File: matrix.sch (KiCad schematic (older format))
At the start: 134 parts, among them SW1 SW_Push, SW10 SW_Push, SW11 SW_Push, SW12 SW_Push, SW13 SW_Push, SW14 SW_Push, SW15 SW_Push, SW16 SW_Push, SW17 SW_Push, SW18 SW_Push, SW19 SW_Push, SW2 SW_Push, SW20 SW_Push, SW21 SW_Push, SW22 SW_Push, SW23 SW_Push, SW24 SW_Push, SW25 SW_Push, SW26 SW_Push, SW27 SW_Push, SW28 SW_Push, SW29 SW_Push, SW3 SW_Push, SW30 SW_Push, SW31 SW_Push, SW32 SW_Push, SW33 SW_Push, SW34 SW_Push, SW35 SW_Push, SW36 SW_Push, SW37 SW_Push, SW38 SW_Push, SW39 SW_Push, SW4 SW_Push, SW40 SW_Push, SW41 SW_Push, SW42 SW_Push, SW43 SW_Push, SW44 SW_Push, SW45 SW_Push, SW46 SW_Push, SW47 SW_Push, SW48 SW_Push, SW49 SW_Push, SW5 SW_Push, SW50 SW_Push, SW51 SW_Push, SW52 SW_Push, SW53 SW_Push, SW54 SW_Push, SW55 SW_Push, SW56 SW_Push, SW57 SW_Push, SW58 SW_Push, SW59 SW_Push, SW6 SW_Push, SW60 SW_Push, SW61 SW_Push, SW62 SW_Push, SW63 SW_Push, SW64 SW_Push, SW65 SW_Push, SW66 SW_Push, SW67 SW_Push, SW7 SW_Push, SW8 SW_Push, SW9 SW_Push

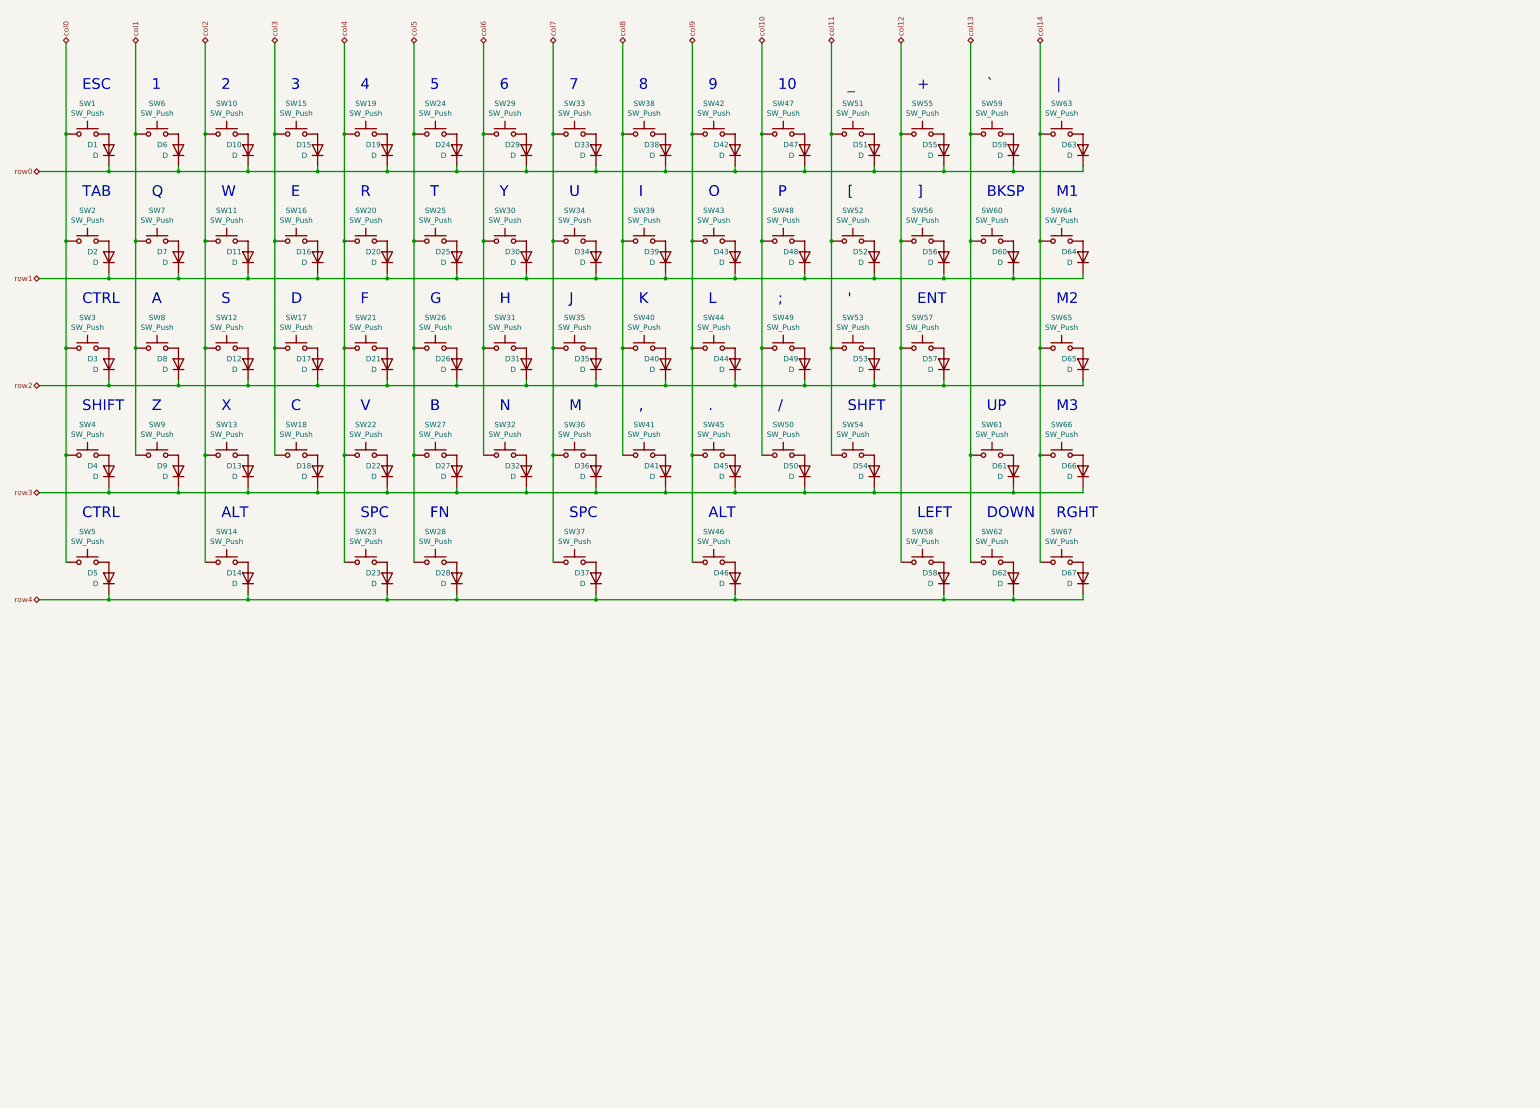
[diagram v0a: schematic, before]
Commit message: added footprints
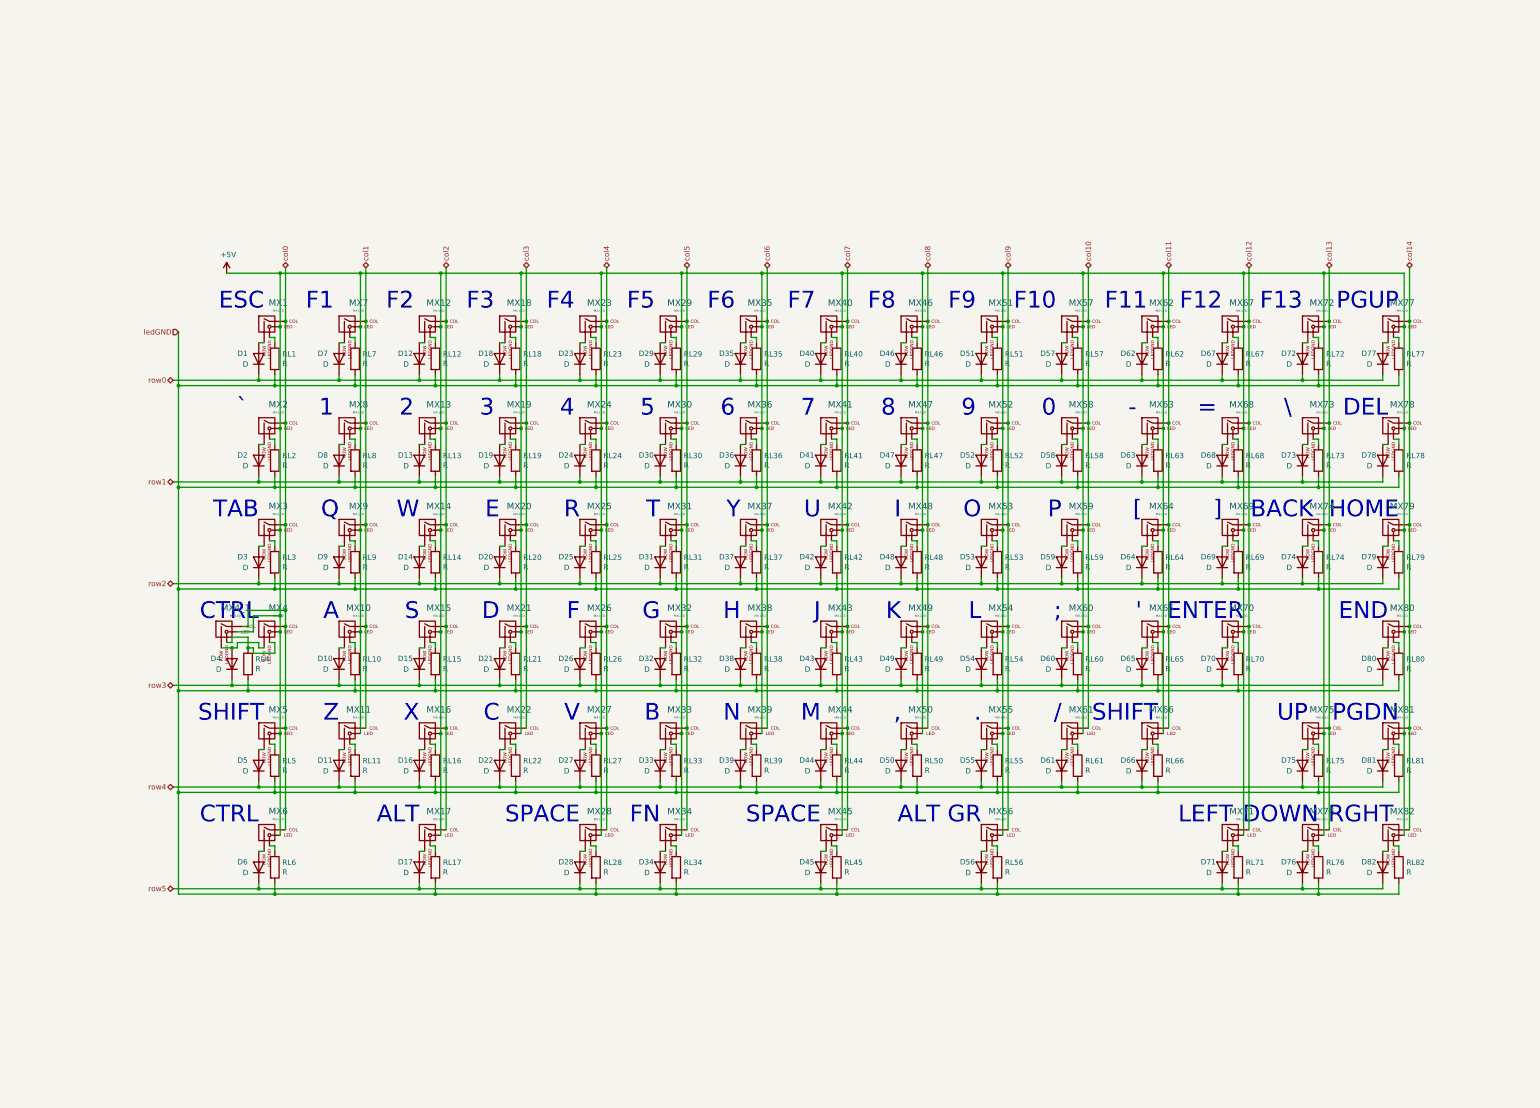
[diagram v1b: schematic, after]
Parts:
- removed SW1, SW10, SW11, SW12, SW13, SW15, SW16, SW17, SW18, SW19, SW20, SW21, SW22, SW24, SW25, SW26, SW27, SW28, SW29, SW30, SW31, SW32, SW33, SW34, SW35, SW36, SW38, SW39, SW40, SW41, SW42, SW43, SW44, SW45, SW47, SW48, SW49, SW50, SW51, SW52, SW53, SW55, SW56, SW58, SW59, SW6, SW61, SW62, SW63, SW64, SW65, SW66, SW67, SW7, SW8, SW9: SW_Push, Fate_Parts:SW_Cherry_MX_1.00u_PCB, symbol Switch:SW_Push
- removed SW14, SW2, SW46, SW5, SW60: SW_Push, Fate_Parts:SW_Cherry_MX_1.50u_PCB, symbol Switch:SW_Push
- removed SW23: SW_Push, Fate_Parts:SW_Cherry_MX_2.00u_PCB_ReversedStabilizers, symbol Switch:SW_Push
- removed SW3, SW54: SW_Push, Fate_Parts:SW_Cherry_MX_1.75u_PCB, symbol Switch:SW_Push
- removed SW37: SW_Push, Fate_Parts:SW_Cherry_MX_2.75u_PCB_ReversedStabilizers, symbol Switch:SW_Push
- removed SW4: SW_Push, Fate_Parts:SW_Cherry_MX_2.25u_PCB, symbol Switch:SW_Push
- removed SW57: SW_Push, Fate_Parts:SW_Cherry_MX_2.25u_PCB_ReversedStabilizers, symbol Switch:SW_Push
- added D68, D69, D70, D71, D72, D73, D74, D75, D76, D77, D78, D79, D80, D81, D82: D, Diode_SMD:D_SOD-123, symbol Device:D
- added MX1, MX10, MX11, MX12, MX13, MX14, MX15, MX16, MX18, MX19, MX2, MX20, MX21, MX22, MX23, MX24, MX25, MX26, MX27, MX29, MX30, MX31, MX32, MX33, MX34, MX35, MX36, MX37, MX38, MX39, MX40, MX41, MX42, MX43, MX44, MX46, MX47, MX48, MX49, MX50, MX51, MX52, MX53, MX54, MX55, MX57, MX58, MX59, MX60, MX61, MX62, MX63, MX64, MX65, MX67, MX68, MX69, MX7, MX71, MX72, MX73, MX75, MX76, MX77, MX78, MX79, MX8, MX80, MX81, MX82, MX9: MX-LED, ai03-MX_only:MXOnly-1U, symbol ai03-schematic_library:MX-LED
- added MX17, MX3, MX56, MX6, MX74: MX-LED, ai03-MX_only:MXOnly-1.5U, symbol ai03-schematic_library:MX-LED
- added MX28: MX-LED, ai03-MX_only:MXOnly-2U-FLIPPED-ReversedStabilizers, symbol ai03-schematic_library:MX-LED
- added MX4, MX66: MX-LED, ai03-MX_only:MXOnly-1.75U, symbol ai03-schematic_library:MX-LED
- added MX45: MX-LED, ai03-MX_only:MXOnly-2.75U-ReversedStabilizers, symbol ai03-schematic_library:MX-LED
- added MX4_1: MX-LED, ai03-MX_only:MXOnly-1.75U-FLIPPED, symbol ai03-schematic_library:MX-LED
- added MX5: MX-LED, ai03-MX_only:MXOnly-2.25U, symbol ai03-schematic_library:MX-LED
- added MX70: MX-LED, ai03-MX_only:MXOnly-2.25U-FLIPPED-ReversedStabilizers, symbol ai03-schematic_library:MX-LED
- added RL1, RL10, RL11, RL12, RL13, RL14, RL15, RL16, RL17, RL18, RL19, RL2, RL20, RL21, RL22, RL23, RL24, RL25, RL26, RL27, RL28, RL29, RL3, RL30, RL31, RL32, RL33, RL34, RL35, RL36, RL37, RL38, RL39, RL4, RL40, RL41, RL42, RL43, RL44, RL45, RL46, RL47, RL48, RL49, RL5, RL50, RL51, RL52, RL53, RL54, RL55, RL56, RL57, RL58, RL59, RL6, RL60, RL61, RL62, RL63, RL64, RL65, RL66, RL67, RL68, RL69, RL7, RL70, RL71, RL72, RL73, RL74, RL75, RL76, RL77, RL78, RL79, RL8, RL80, RL81, RL82, RL9: R, Resistor_SMD:R_0805_2012Metric_Pad1.15x1.40mm_HandSolder, symbol Device:R
- D1, D10, D11, D12, D13, D14, D15, D16, D17, D18, D19, D2, D20, D21, D22, D23, D24, D25, D26, D27, D28, D29, D3, D30, D31, D32, D33, D34, D35, D36, D37, D38, D39, D4, D40, D41, D42, D43, D44, D45, D46, D47, D48, D49, D5, D50, D51, D52, D53, D54, D55, D56, D57, D58, D59, D6, D60, D61, D62, D63, D64, D65, D66, D67, D7, D8, D9: footprint Diodes_SMD:D_SOD-123 -> Diode_SMD:D_SOD-123
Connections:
- net col0: now also MX1.1 (COL), MX2.1 (COL), MX3.1 (COL), MX4.1 (COL), MX4_1.1 (COL), MX5.1 (COL), MX6.1 (COL)
- net col1: now also MX10.1 (COL), MX11.1 (COL), MX7.1 (COL), MX8.1 (COL), MX9.1 (COL)
- net col10: now also MX57.1 (COL), MX58.1 (COL), MX59.1 (COL), MX60.1 (COL), MX61.1 (COL)
- net col11: now also MX62.1 (COL), MX63.1 (COL), MX64.1 (COL), MX65.1 (COL), MX66.1 (COL)
- net col12: now also MX67.1 (COL), MX68.1 (COL), MX69.1 (COL), MX70.1 (COL), MX71.1 (COL)
- net col13: now also MX72.1 (COL), MX73.1 (COL), MX74.1 (COL), MX75.1 (COL), MX76.1 (COL)
- net col14: now also MX77.1 (COL), MX78.1 (COL), MX79.1 (COL), MX80.1 (COL), MX81.1 (COL), MX82.1 (COL)
- net col2: now also MX12.1 (COL), MX13.1 (COL), MX14.1 (COL), MX15.1 (COL), MX16.1 (COL), MX17.1 (COL)
- net col3: now also MX18.1 (COL), MX19.1 (COL), MX20.1 (COL), MX21.1 (COL), MX22.1 (COL)
- net col4: now also MX23.1 (COL), MX24.1 (COL), MX25.1 (COL), MX26.1 (COL), MX27.1 (COL), MX28.1 (COL)
- net col5: now also MX29.1 (COL), MX30.1 (COL), MX31.1 (COL), MX32.1 (COL), MX33.1 (COL), MX34.1 (COL)
- net col6: now also MX35.1 (COL), MX36.1 (COL), MX37.1 (COL), MX38.1 (COL), MX39.1 (COL)
- net col7: now also MX40.1 (COL), MX41.1 (COL), MX42.1 (COL), MX43.1 (COL), MX44.1 (COL), MX45.1 (COL)
- net col8: now also MX46.1 (COL), MX47.1 (COL), MX48.1 (COL), MX49.1 (COL), MX50.1 (COL)
- net col9: now also MX51.1 (COL), MX52.1 (COL), MX53.1 (COL), MX54.1 (COL), MX55.1 (COL), MX56.1 (COL)
- net row0: now also D12.1 (K), D18.1 (K), D23.1 (K), D35.1 (K), D40.1 (K), D46.1 (K), D57.1 (K), D62.1 (K), D67.1 (K), D7.1 (K), D72.1 (K), D77.1 (K); no longer D10.1 (K), D15.1 (K), D19.1 (K), D24.1 (K), D33.1 (K), D38.1 (K), D42.1 (K), D47.1 (K), D55.1 (K), D59.1 (K), D6.1 (K), D63.1 (K)
- net row1: now also D13.1 (K), D19.1 (K), D24.1 (K), D36.1 (K), D41.1 (K), D47.1 (K), D58.1 (K), D63.1 (K), D8.1 (K), D68.1 (K), D73.1 (K), D78.1 (K); no longer D11.1 (K), D16.1 (K), D20.1 (K), D25.1 (K), D34.1 (K), D39.1 (K), D43.1 (K), D48.1 (K), D56.1 (K), D60.1 (K), D64.1 (K), D7.1 (K)
- net row2: now also D14.1 (K), D20.1 (K), D25.1 (K), D37.1 (K), D42.1 (K), D48.1 (K), D59.1 (K), D64.1 (K), D9.1 (K), D69.1 (K), D74.1 (K), D79.1 (K); no longer D12.1 (K), D17.1 (K), D21.1 (K), D26.1 (K), D35.1 (K), D40.1 (K), D44.1 (K), D49.1 (K), D57.1 (K), D65.1 (K), D8.1 (K)
- net row3: now also D10.1 (K), D15.1 (K), D21.1 (K), D26.1 (K), D38.1 (K), D43.1 (K), D49.1 (K), D60.1 (K), D65.1 (K), D70.1 (K), D80.1 (K); no longer D13.1 (K), D18.1 (K), D22.1 (K), D27.1 (K), D36.1 (K), D41.1 (K), D45.1 (K), D50.1 (K), D61.1 (K), D66.1 (K), D9.1 (K)
- net row4: now also D11.1 (K), D16.1 (K), D22.1 (K), D27.1 (K), D33.1 (K), D39.1 (K), D44.1 (K), D50.1 (K), D55.1 (K), D61.1 (K), D66.1 (K), D75.1 (K), D81.1 (K); no longer D14.1 (K), D23.1 (K), D28.1 (K), D37.1 (K), D46.1 (K), D58.1 (K), D62.1 (K), D67.1 (K)
- net at D1.2 (A): now also MX1.2 (ROW)
- net at D6.2 (A): now also MX6.2 (ROW)
- net at D2.2 (A): now also MX2.2 (ROW)
- net at D7.2 (A): now also MX7.2 (ROW)
- net at D3.2 (A): now also MX3.2 (ROW)
- net at D4.2 (A): now also MX4.2 (ROW), MX4_1.2 (ROW)
- net at D5.2 (A): now also MX5.2 (ROW)
- net at D8.2 (A): now also MX8.2 (ROW)
- net at D9.2 (A): now also MX9.2 (ROW)
- net at D10.2 (A): now also MX10.2 (ROW)
- net at D11.2 (A): now also MX11.2 (ROW)
- net at D12.2 (A): now also MX12.2 (ROW)
- net at D13.2 (A): now also MX13.2 (ROW)
- net at D14.2 (A): now also MX14.2 (ROW)
- net at D15.2 (A): now also MX15.2 (ROW)
- net at D16.2 (A): now also MX16.2 (ROW)
- net at D17.2 (A): now also MX17.2 (ROW)
- net at D18.2 (A): now also MX18.2 (ROW)
- net at D19.2 (A): now also MX19.2 (ROW)
- net at D20.2 (A): now also MX20.2 (ROW)
- net at D21.2 (A): now also MX21.2 (ROW)
- net at D22.2 (A): now also MX22.2 (ROW)
- net at D23.2 (A): now also MX23.2 (ROW)
- net at D24.2 (A): now also MX24.2 (ROW)
- net at D25.2 (A): now also MX25.2 (ROW)
- net at D26.2 (A): now also MX26.2 (ROW)
- net at D27.2 (A): now also MX27.2 (ROW)
- net at D28.2 (A): now also MX28.2 (ROW)
- net at D29.2 (A): now also MX29.2 (ROW)
- net at D30.2 (A): now also MX30.2 (ROW)
- net at D31.2 (A): now also MX31.2 (ROW)
- net at D32.2 (A): now also MX32.2 (ROW)
- net at D33.2 (A): now also MX33.2 (ROW)
- net at D34.2 (A): now also MX34.2 (ROW)
- net at D35.2 (A): now also MX35.2 (ROW)
- net at D36.2 (A): now also MX36.2 (ROW)
- net at D37.2 (A): now also MX37.2 (ROW)
- net at D38.2 (A): now also MX38.2 (ROW)
- net at D39.2 (A): now also MX39.2 (ROW)
- net at D40.2 (A): now also MX40.2 (ROW)
- net at D41.2 (A): now also MX41.2 (ROW)
- net at D42.2 (A): now also MX42.2 (ROW)
- net at D43.2 (A): now also MX43.2 (ROW)
- net at D44.2 (A): now also MX44.2 (ROW)
- net at D45.2 (A): now also MX45.2 (ROW)
- net at D46.2 (A): now also MX46.2 (ROW)
- net at D47.2 (A): now also MX47.2 (ROW)
- net at D48.2 (A): now also MX48.2 (ROW)
- net at D49.2 (A): now also MX49.2 (ROW)
- net at D50.2 (A): now also MX50.2 (ROW)
- net at D51.2 (A): now also MX51.2 (ROW)
- net at D52.2 (A): now also MX52.2 (ROW)
- net at D53.2 (A): now also MX53.2 (ROW)
- net at D54.2 (A): now also MX54.2 (ROW)
- net at D55.2 (A): now also MX55.2 (ROW)
- net at D56.2 (A): now also MX56.2 (ROW)
- net at D57.2 (A): now also MX57.2 (ROW)
- net at D58.2 (A): now also MX58.2 (ROW)
- net at D59.2 (A): now also MX59.2 (ROW)
- net at D60.2 (A): now also MX60.2 (ROW)
- net at D61.2 (A): now also MX61.2 (ROW)
- net at D62.2 (A): now also MX62.2 (ROW)
- net at D63.2 (A): now also MX63.2 (ROW)
- net at D64.2 (A): now also MX64.2 (ROW)
- net at D65.2 (A): now also MX65.2 (ROW)
- net at D66.2 (A): now also MX66.2 (ROW)
- net at D67.2 (A): now also MX67.2 (ROW)
- new net: MX4.4 (LEDGND), MX4_1.4 (LEDGND), RL4.1
- new net: MX1.4 (LEDGND), RL1.1
- new net: MX7.4 (LEDGND), RL7.1
- new net: MX12.4 (LEDGND), RL12.1
- new net: MX18.4 (LEDGND), RL18.1
- new net: MX40.4 (LEDGND), RL40.1
- new net: MX35.4 (LEDGND), RL35.1
- new net: MX23.4 (LEDGND), RL23.1
- new net: MX29.4 (LEDGND), RL29.1
- new net: MX62.4 (LEDGND), RL62.1
- new net: MX57.4 (LEDGND), RL57.1
- new net: MX46.4 (LEDGND), RL46.1
- new net: MX51.4 (LEDGND), RL51.1
- new net: D77.2 (A), MX77.2 (ROW)
- new net: MX77.4 (LEDGND), RL77.1
- new net: MX67.4 (LEDGND), RL67.1
- new net: D72.2 (A), MX72.2 (ROW)
- new net: MX72.4 (LEDGND), RL72.1
- new net: MX5.4 (LEDGND), RL5.1
- new net: D78.2 (A), MX78.2 (ROW)
- new net: MX68.4 (LEDGND), RL68.1
- new net: MX73.4 (LEDGND), RL73.1
- new net: MX78.4 (LEDGND), RL78.1
- new net: D68.2 (A), MX68.2 (ROW)
- new net: D73.2 (A), MX73.2 (ROW)
- new net: MX58.4 (LEDGND), RL58.1
- new net: MX52.4 (LEDGND), RL52.1
- new net: MX47.4 (LEDGND), RL47.1
- new net: MX19.4 (LEDGND), RL19.1
- new net: MX30.4 (LEDGND), RL30.1
- new net: MX24.4 (LEDGND), RL24.1
- new net: MX63.4 (LEDGND), RL63.1
- new net: MX36.4 (LEDGND), RL36.1
- new net: MX13.4 (LEDGND), RL13.1
- new net: MX41.4 (LEDGND), RL41.1
- new net: MX2.4 (LEDGND), RL2.1
- new net: MX8.4 (LEDGND), RL8.1
- new net: D79.2 (A), MX79.2 (ROW)
- new net: MX69.4 (LEDGND), RL69.1
- new net: MX74.4 (LEDGND), RL74.1
- new net: MX79.4 (LEDGND), RL79.1
- new net: D69.2 (A), MX69.2 (ROW)
- new net: D74.2 (A), MX74.2 (ROW)
- new net: MX59.4 (LEDGND), RL59.1
- new net: MX53.4 (LEDGND), RL53.1
- new net: MX48.4 (LEDGND), RL48.1
- new net: MX20.4 (LEDGND), RL20.1
- new net: MX31.4 (LEDGND), RL31.1
- new net: MX25.4 (LEDGND), RL25.1
- new net: MX64.4 (LEDGND), RL64.1
- new net: MX37.4 (LEDGND), RL37.1
- new net: MX14.4 (LEDGND), RL14.1
- new net: MX42.4 (LEDGND), RL42.1
- new net: MX3.4 (LEDGND), RL3.1
- new net: MX9.4 (LEDGND), RL9.1
- new net: D80.2 (A), MX80.2 (ROW)
- new net: MX70.4 (LEDGND), RL70.1
- new net: MX80.4 (LEDGND), RL80.1
- new net: D70.2 (A), MX70.2 (ROW)
- new net: MX60.4 (LEDGND), RL60.1
- new net: MX54.4 (LEDGND), RL54.1
- new net: MX49.4 (LEDGND), RL49.1
- new net: MX21.4 (LEDGND), RL21.1
- new net: MX32.4 (LEDGND), RL32.1
- new net: MX26.4 (LEDGND), RL26.1
- new net: MX65.4 (LEDGND), RL65.1
- new net: MX38.4 (LEDGND), RL38.1
- new net: MX15.4 (LEDGND), RL15.1
- new net: MX43.4 (LEDGND), RL43.1
- new net: MX10.4 (LEDGND), RL10.1
- new net: D81.2 (A), MX81.2 (ROW)
- new net: MX75.4 (LEDGND), RL75.1
- new net: MX81.4 (LEDGND), RL81.1
- new net: D75.2 (A), MX75.2 (ROW)
- new net: MX61.4 (LEDGND), RL61.1
- new net: MX55.4 (LEDGND), RL55.1
- new net: MX50.4 (LEDGND), RL50.1
- new net: MX22.4 (LEDGND), RL22.1
- new net: MX33.4 (LEDGND), RL33.1
- new net: MX27.4 (LEDGND), RL27.1
- new net: MX66.4 (LEDGND), RL66.1
- new net: MX39.4 (LEDGND), RL39.1
- new net: MX16.4 (LEDGND), RL16.1
- new net: MX44.4 (LEDGND), RL44.1
- new net: MX11.4 (LEDGND), RL11.1
- new net: D82.2 (A), MX82.2 (ROW)
- new net: MX71.4 (LEDGND), RL71.1
- new net: MX76.4 (LEDGND), RL76.1
- new net: MX82.4 (LEDGND), RL82.1
- new net: D71.2 (A), MX71.2 (ROW)
- new net: D76.2 (A), MX76.2 (ROW)
- new net: MX56.4 (LEDGND), RL56.1
- new net: MX34.4 (LEDGND), RL34.1
- new net: MX28.4 (LEDGND), RL28.1
- new net: MX17.4 (LEDGND), RL17.1
- new net: MX45.4 (LEDGND), RL45.1
- new net: MX6.4 (LEDGND), RL6.1
- new net +5V: MX1.3 (LED), MX10.3 (LED), MX11.3 (LED), MX12.3 (LED), MX13.3 (LED), MX14.3 (LED), MX15.3 (LED), MX16.3 (LED), MX17.3 (LED), MX18.3 (LED), MX19.3 (LED), MX2.3 (LED), MX20.3 (LED), MX21.3 (LED), MX22.3 (LED), MX23.3 (LED), MX24.3 (LED), MX25.3 (LED), MX26.3 (LED), MX27.3 (LED), MX28.3 (LED), MX29.3 (LED), MX3.3 (LED), MX30.3 (LED), MX31.3 (LED), MX32.3 (LED), MX33.3 (LED), MX34.3 (LED), MX35.3 (LED), MX36.3 (LED), MX37.3 (LED), MX38.3 (LED), MX39.3 (LED), MX4.3 (LED), MX40.3 (LED), MX41.3 (LED), MX42.3 (LED), MX43.3 (LED), MX44.3 (LED), MX45.3 (LED), MX46.3 (LED), MX47.3 (LED), MX48.3 (LED), MX49.3 (LED), MX4_1.3 (LED), MX5.3 (LED), MX50.3 (LED), MX51.3 (LED), MX52.3 (LED), MX53.3 (LED), MX54.3 (LED), MX55.3 (LED), MX56.3 (LED), MX57.3 (LED), MX58.3 (LED), MX59.3 (LED), MX6.3 (LED), MX60.3 (LED), MX61.3 (LED), MX62.3 (LED), MX63.3 (LED), MX64.3 (LED), MX65.3 (LED), MX66.3 (LED), MX67.3 (LED), MX68.3 (LED), MX69.3 (LED), MX7.3 (LED), MX70.3 (LED), MX71.3 (LED), MX72.3 (LED), MX73.3 (LED), MX74.3 (LED), MX75.3 (LED), MX76.3 (LED), MX77.3 (LED), MX78.3 (LED), MX79.3 (LED), MX8.3 (LED), MX80.3 (LED), MX81.3 (LED), MX82.3 (LED), MX9.3 (LED)
- new net ledGND: RL1.2, RL10.2, RL11.2, RL12.2, RL13.2, RL14.2, RL15.2, RL16.2, RL17.2, RL18.2, RL19.2, RL2.2, RL20.2, RL21.2, RL22.2, RL23.2, RL24.2, RL25.2, RL26.2, RL27.2, RL28.2, RL29.2, RL3.2, RL30.2, RL31.2, RL32.2, RL33.2, RL34.2, RL35.2, RL36.2, RL37.2, RL38.2, RL39.2, RL4.2, RL40.2, RL41.2, RL42.2, RL43.2, RL44.2, RL45.2, RL46.2, RL47.2, RL48.2, RL49.2, RL5.2, RL50.2, RL51.2, RL52.2, RL53.2, RL54.2, RL55.2, RL56.2, RL57.2, RL58.2, RL59.2, RL6.2, RL60.2, RL61.2, RL62.2, RL63.2, RL64.2, RL65.2, RL66.2, RL67.2, RL68.2, RL69.2, RL7.2, RL70.2, RL71.2, RL72.2, RL73.2, RL74.2, RL75.2, RL76.2, RL77.2, RL78.2, RL79.2, RL8.2, RL80.2, RL81.2, RL82.2, RL9.2
- new net row5: D17.1 (K), D28.1 (K), D34.1 (K), D45.1 (K), D56.1 (K), D6.1 (K), D71.1 (K), D76.1 (K), D82.1 (K)
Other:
- note added: "-"
- note added: "."
- note added: "0"
- note added: "="
- note added: "ALT GR"
- note added: "BACK"
- note added: "DEL"
- note added: "END"
- note added: "ENTER"
- note added: "F1"
- note added: "F10"
- note added: "F11"
- note added: "F12"
- note added: "F13"
- note added: "F2"
- note added: "F3"
- note added: "F4"
- note added: "F5"
- note added: "F6"
- note added: "F7"
- note added: "F8"
- note added: "F9"
- note added: "HOME"
- note added: "PGDN"
- note added: "PGUP"
- note added: "RGHT"
- note added: "SPACE"
- note added: "\"
- note removed: "+"
- note removed: ".\n"
- note removed: "10"
- note removed: "BKSP"
- note removed: "ENT"
- note removed: "M1"
- note removed: "M2"
- note removed: "M3"
- note removed: "RGHT\n"
- note removed: "SHFT"
- note removed: "SPC"
- note removed: "_"
- note removed: "|"

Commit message: added column and row routing
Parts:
- MX28: footprint ai03-MX_only:MXOnly-2U-FLIPPED-ReversedStabilizers -> ai03-MX_only:MXOnly-2U-ReversedStabilizers
- MX70: footprint ai03-MX_only:MXOnly-2.25U-FLIPPED-ReversedStabilizers -> ai03-MX_only:MXOnly-2.25U-ReversedStabilizers
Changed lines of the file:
@@
 F 0 "MX70" H 12182 6473 60  0000 C CNN
 F 1 "MX-LED" H 12182 6399 20  0000 C CNN
-F 2 "ai03-MX_only:MXOnly-2.25U-FLIPPED-ReversedStabilizers" H 11475 6225 60  0001 C CNN
+F 2 "ai03-MX_only:MXOnly-2.25U-ReversedStabilizers" H 11475 6225 60  0001 C CNN
 F 3 "" H 11475 6225 60  0001 C CNN
 	1    12100 6250
@@
 F 0 "MX28" H 6182 8373 60  0000 C CNN
 F 1 "MX-LED" H 6182 8299 20  0000 C CNN
-F 2 "ai03-MX_only:MXOnly-2U-FLIPPED-ReversedStabilizers" H 5475 8125 60  0001 C CNN
+F 2 "ai03-MX_only:MXOnly-2U-ReversedStabilizers" H 5475 8125 60  0001 C CNN
 F 3 "" H 5475 8125 60  0001 C CNN
 	1    6100 8150

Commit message: finished pcb v2
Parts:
- added LS1, LS10, LS11, LS12, LS13, LS14, LS15, LS16, LS17, LS2, LS3, LS4, LS5, LS6, LS7, LS8, LS9: LED, LED_SMD:LED_0805_2012Metric_Pad1.15x1.40mm_HandSolder, symbol Device:LED
- added RS1, RS10, RS11, RS12, RS13, RS14, RS15, RS16, RS17, RS2, RS3, RS4, RS5, RS6, RS7, RS8, RS9: R, Resistor_SMD:R_0805_2012Metric_Pad1.15x1.40mm_HandSolder, symbol Device:R
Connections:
- net ledGND: now also RS1.1, RS10.1, RS11.1, RS12.1, RS13.1, RS14.1, RS15.1, RS16.1, RS17.1, RS2.1, RS3.1, RS4.1, RS5.1, RS6.1, RS7.1, RS8.1, RS9.1
- net +5V renamed VCC
- net VCC: now also LS1.2 (A), LS10.2 (A), LS11.2 (A), LS12.2 (A), LS13.2 (A), LS14.2 (A), LS15.2 (A), LS16.2 (A), LS17.2 (A), LS2.2 (A), LS3.2 (A), LS4.2 (A), LS5.2 (A), LS6.2 (A), LS7.2 (A), LS8.2 (A), LS9.2 (A)
- new net: LS12.1 (K), RS12.2
- new net: LS11.1 (K), RS11.2
- new net: LS8.1 (K), RS8.2
- new net: LS7.1 (K), RS7.2
- new net: LS6.1 (K), RS6.2
- new net: LS5.1 (K), RS5.2
- new net: LS4.1 (K), RS4.2
- new net: LS2.1 (K), RS2.2
- new net: LS1.1 (K), RS1.2
- new net: LS16.1 (K), RS16.2
- new net: LS15.1 (K), RS15.2
- new net: LS17.1 (K), RS17.2
- new net: LS14.1 (K), RS14.2
- new net: LS10.1 (K), RS10.2
- new net: LS3.1 (K), RS3.2
- new net: LS9.1 (K), RS9.2
- new net: LS13.1 (K), RS13.2
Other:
- moved on the sheet: D1, D10, D11, D12, D13, D14, D15, D16, D17, D18, D19, D2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
